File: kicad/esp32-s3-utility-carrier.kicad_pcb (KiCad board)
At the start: 2 copper layers, 130 x 85 mm, 30 parts, among them SW1 BTN1, SW2 BTN2, SW3 BTN3, U2 SN74AHCT125N

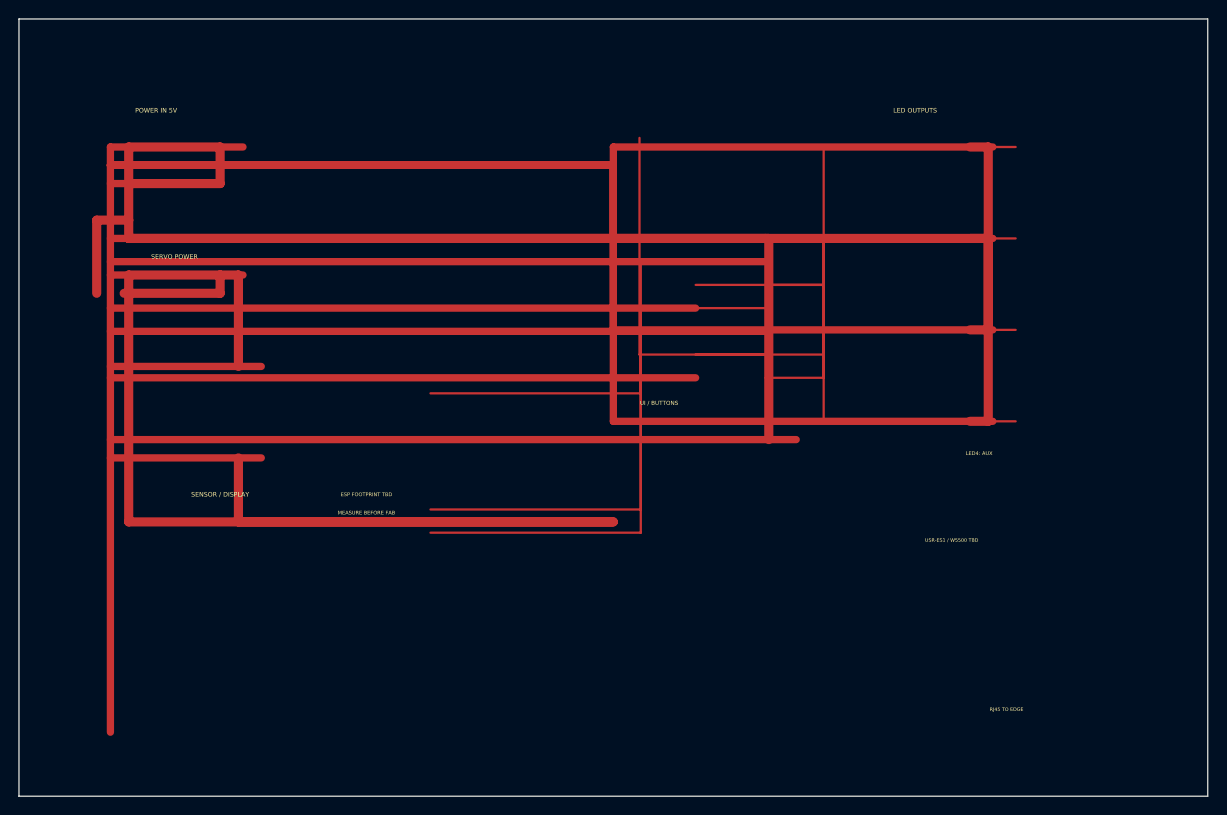
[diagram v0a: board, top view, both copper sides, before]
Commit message: fix(pcb): replace messy routing with LED data routing only
Revert v0.7 board-wide power traces; keep v0.7 placement. Route thin
LED data chain and short C_AHCT at U2 with 45° bends outside ESP keep-outs.

Co-authored-by: Cursor <cursoragent@cursor.com>
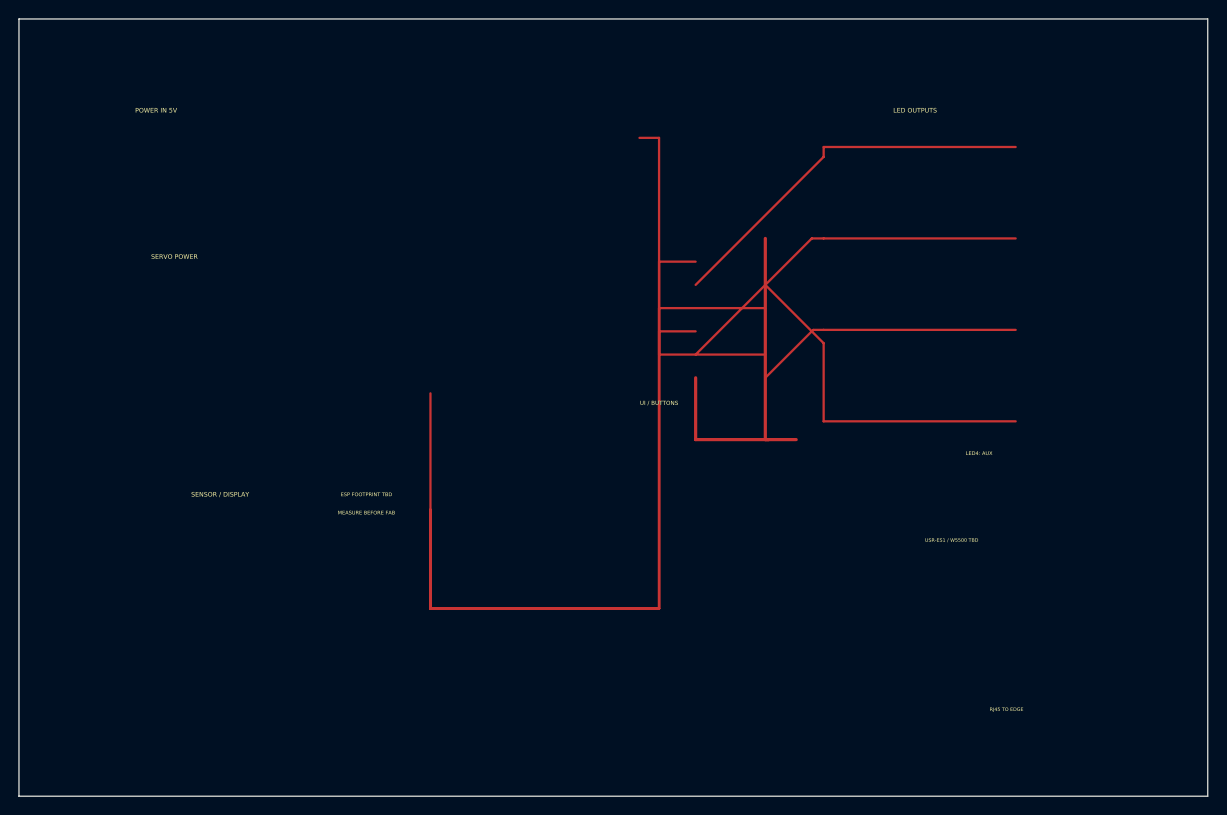
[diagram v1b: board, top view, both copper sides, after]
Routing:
- net GND: track 984.2 -> 17.8 mm
- net 5V_SERVO: track 162.5 -> 0.00 mm
- net 5V_LED: track 142.0 -> 0.00 mm
- net 5V_LOGIC: track 94.0 -> 22.4 mm
- net LED4_IN: track 45.9 -> 93.1 mm
- net 5V_MAIN: track 43.5 -> 0.00 mm
- net LED2_IN: track 48.5 -> 70.2 mm
- net LED1_IN: track 58.6 -> 75.3 mm
- net LED1_DATA: track 50.1 -> 41.9 mm
- net LED2_DATA: track 47.7 -> 40.3 mm
- net LED4_DATA: track 42.3 -> 38.6 mm
- net LED3_DATA: track 32.6 -> 29.6 mm
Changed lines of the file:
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@@
     (property "Footprint" "carrier:JST_W5500_1x08_Placeholder")
     (attr through_hole)
-  )  (segment (start 12 18) (end 12.0 18) (width 1.0) (layer "F.Cu") (net 1))
-  (segment (start 12.0 18) (end 22 18) (width 1.0) (layer "F.Cu") (net 1))
-  (segment (start 22 18) (end 22 14) (width 1.0) (layer "F.Cu") (net 1))
-  (segment (start 15.96 18) (end 10.0 18) (width 0.8) (layer "F.Cu") (net 2))
-  (segment (start 24.5 14) (end 10.0 14) (width 0.8) (layer "F.Cu") (net 2))
-  (segment (start 22 14) (end 12.0 14) (width 1.0) (layer "F.Cu") (net 1))
-  (segment (start 12.0 14) (end 12.0 22) (width 1.0) (layer "F.Cu") (net 1))
-  (segment (start 12.0 22) (end 8.5 22) (width 1.0) (layer "F.Cu") (net 1))
-  (segment (start 8.5 22) (end 8.5 30) (width 1.0) (layer "F.Cu") (net 1))
-  (segment (start 12.0 22) (end 12.0 24) (width 1.0) (layer "F.Cu") (net 3))
-  (segment (start 12.0 24) (end 81.62 24) (width 1.0) (layer "F.Cu") (net 3))
-  (segment (start 81.62 24) (end 82 24) (width 1.0) (layer "F.Cu") (net 3))
-  (segment (start 82 24) (end 82 46) (width 1.0) (layer "F.Cu") (net 3))
-  (segment (start 85.0 46) (end 10.0 46) (width 0.8) (layer "F.Cu") (net 2))
-  (segment (start 74 39.24) (end 10.0 39.24) (width 0.8) (layer "F.Cu") (net 2))
-  (segment (start 74 24) (end 10.0 24) (width 0.8) (layer "F.Cu") (net 2))
-  (segment (start 74 31.62) (end 10.0 31.62) (width 0.8) (layer "F.Cu") (net 2))
-  (segment (start 81.62 34.16) (end 10.0 34.16) (width 0.8) (layer "F.Cu") (net 2))
-  (segment (start 81.62 26.54) (end 10.0 26.54) (width 0.8) (layer "F.Cu") (net 2))
-  (segment (start 11.5 30) (end 22 30) (width 1.0) (layer "F.Cu") (net 5))
-  (segment (start 22 30) (end 22 28) (width 1.0) (layer "F.Cu") (net 5))
-  (segment (start 24.5 28) (end 10.0 28) (width 0.8) (layer "F.Cu") (net 2))
-  (segment (start 22 28) (end 24 28) (width 1.0) (layer "F.Cu") (net 5))
-  (segment (start 24 28) (end 24 38) (width 1.0) (layer "F.Cu") (net 5))
-  (segment (start 26.5 38) (end 10.0 38) (width 0.8) (layer "F.Cu") (net 2))
-  (segment (start 22 28) (end 12.0 28) (width 1.0) (layer "F.Cu") (net 5))
-  (segment (start 12.0 28) (end 12.0 55) (width 1.0) (layer "F.Cu") (net 5))
-  (segment (start 12.0 55) (end 65 55) (width 1.0) (layer "F.Cu") (net 5))
-  (segment (start 65 55) (end 24 55) (width 1.0) (layer "F.Cu") (net 5))
-  (segment (start 24 55) (end 24 48) (width 1.0) (layer "F.Cu") (net 5))
-  (segment (start 26.5 48) (end 10.0 48) (width 0.8) (layer "F.Cu") (net 2))
-  (segment (start 106.0 24) (end 106.0 14) (width 1.0) (layer "F.Cu") (net 4))
-  (segment (start 106.0 14) (end 104 14) (width 1.0) (layer "F.Cu") (net 4))
-  (segment (start 106.5 14) (end 65.0 14) (width 0.8) (layer "F.Cu") (net 2))
-  (segment (start 65.0 14) (end 65.0 16) (width 0.8) (layer "F.Cu") (net 2))
-  (segment (start 65.0 16) (end 10.0 16) (width 0.8) (layer "F.Cu") (net 2))
-  (segment (start 106.0 24) (end 106.0 24) (width 1.0) (layer "F.Cu") (net 4))
-  (segment (start 106.0 24) (end 104 24) (width 1.0) (layer "F.Cu") (net 4))
-  (segment (start 106.5 24) (end 65.0 24) (width 0.8) (layer "F.Cu") (net 2))
-  (segment (start 65.0 24) (end 65.0 16) (width 0.8) (layer "F.Cu") (net 2))
-  (segment (start 65.0 16) (end 10.0 16) (width 0.8) (layer "F.Cu") (net 2))
-  (segment (start 106.0 24) (end 106.0 34) (width 1.0) (layer "F.Cu") (net 4))
-  (segment (start 106.0 34) (end 104 34) (width 1.0) (layer "F.Cu") (net 4))
-  (segment (start 106.5 34) (end 65.0 34) (width 0.8) (layer "F.Cu") (net 2))
-  (segment (start 65.0 34) (end 65.0 16) (width 0.8) (layer "F.Cu") (net 2))
-  (segment (start 65.0 16) (end 10.0 16) (width 0.8) (layer "F.Cu") (net 2))
-  (segment (start 106.0 24) (end 106.0 44) (width 1.0) (layer "F.Cu") (net 4))
-  (segment (start 106.0 44) (end 104 44) (width 1.0) (layer "F.Cu") (net 4))
-  (segment (start 106.5 44) (end 65.0 44) (width 0.8) (layer "F.Cu") (net 2))
-  (segment (start 65.0 44) (end 65.0 16) (width 0.8) (layer "F.Cu") (net 2))
-  (segment (start 65.0 16) (end 10.0 16) (width 0.8) (layer "F.Cu") (net 2))
-  (segment (start 12.0 24) (end 106.0 24) (width 1.0) (layer "F.Cu") (net 4))
-  (segment (start 45 56.18) (end 68.0 56.18) (width 0.25) (layer "F.Cu") (net 7))
-  (segment (start 68.0 56.18) (end 68.0 26.54) (width 0.25) (layer "F.Cu") (net 7))
-  (segment (start 68.0 26.54) (end 74 26.54) (width 0.25) (layer "F.Cu") (net 7))
-  (segment (start 74 29.08) (end 88 29.08) (width 0.25) (layer "F.Cu") (net 8))
-  (segment (start 88 29.08) (end 88 14) (width 0.25) (layer "F.Cu") (net 8))
-  (segment (start 88 14) (end 100.0 14) (width 0.25) (layer "F.Cu") (net 8))
-  (segment (start 100.0 14) (end 109.0 14) (width 0.25) (layer "F.Cu") (net 8))
-  (segment (start 45 53.64) (end 68.0 53.64) (width 0.25) (layer "F.Cu") (net 9))
-  (segment (start 68.0 53.64) (end 68.0 34.16) (width 0.25) (layer "F.Cu") (net 9))
-  (segment (start 68.0 34.16) (end 74 34.16) (width 0.25) (layer "F.Cu") (net 9))
-  (segment (start 74 36.7) (end 88 36.7) (width 0.25) (layer "F.Cu") (net 10))
-  (segment (start 88 36.7) (end 88 24) (width 0.25) (layer "F.Cu") (net 10))
-  (segment (start 88 24) (end 100.0 24) (width 0.25) (layer "F.Cu") (net 10))
-  (segment (start 100.0 24) (end 109.0 24) (width 0.25) (layer "F.Cu") (net 10))
-  (segment (start 67.86 13.0) (end 67.86 36.7) (width 0.25) (layer "F.Cu") (net 11))
-  (segment (start 67.86 36.7) (end 68.0 36.7) (width 0.25) (layer "F.Cu") (net 11))
-  (segment (start 68.0 36.7) (end 81.62 36.7) (width 0.25) (layer "F.Cu") (net 11))
-  (segment (start 81.62 39.24) (end 88 39.24) (width 0.25) (layer "F.Cu") (net 12))
-  (segment (start 88 39.24) (end 88 34) (width 0.25) (layer "F.Cu") (net 12))
-  (segment (start 88 34) (end 100.0 34) (width 0.25) (layer "F.Cu") (net 12))
-  (segment (start 100.0 34) (end 109.0 34) (width 0.25) (layer "F.Cu") (net 12))
-  (segment (start 45 40.94) (end 68.0 40.94) (width 0.25) (layer "F.Cu") (net 13))
-  (segment (start 68.0 40.94) (end 68.0 31.62) (width 0.25) (layer "F.Cu") (net 13))
-  (segment (start 68.0 31.62) (end 81.62 31.62) (width 0.25) (layer "F.Cu") (net 13))
-  (segment (start 81.62 29.08) (end 88 29.08) (width 0.25) (layer "F.Cu") (net 14))
-  (segment (start 88 29.08) (end 88 44) (width 0.25) (layer "F.Cu") (net 14))
-  (segment (start 88 44) (end 100.0 44) (width 0.25) (layer "F.Cu") (net 14))
-  (segment (start 100.0 44) (end 109.0 44) (width 0.25) (layer "F.Cu") (net 14))
-  (segment (start 10.0 14) (end 10.0 78) (width 0.8) (layer "F.Cu") (net 2))
+  )  (segment (start 45 56.18) (end 45 64.5) (width 0.25) (layer "F.Cu") (net 7))
+  (segment (start 45 64.5) (end 70.0 64.5) (width 0.25) (layer "F.Cu") (net 7))
+  (segment (start 70.0 64.5) (end 70.0 26.54) (width 0.25) (layer "F.Cu") (net 7))
+  (segment (start 70.0 26.54) (end 74 26.54) (width 0.25) (layer "F.Cu") (net 7))
+  (segment (start 74 29.08) (end 88.0 15.079999999999998) (width 0.25) (layer "F.Cu") (net 8))
+  (segment (start 88.0 15.079999999999998) (end 88 14) (width 0.25) (layer "F.Cu") (net 8))
+  (segment (start 88 14) (end 109.0 14) (width 0.25) (layer "F.Cu") (net 8))
+  (segment (start 45 53.64) (end 45 64.5) (width 0.25) (layer "F.Cu") (net 9))
+  (segment (start 45 64.5) (end 70.0 64.5) (width 0.25) (layer "F.Cu") (net 9))
+  (segment (start 70.0 64.5) (end 70.0 34.16) (width 0.25) (layer "F.Cu") (net 9))
+  (segment (start 70.0 34.16) (end 74 34.16) (width 0.25) (layer "F.Cu") (net 9))
+  (segment (start 74 36.7) (end 86.7 24.0) (width 0.25) (layer "F.Cu") (net 10))
+  (segment (start 86.7 24.0) (end 88 24) (width 0.25) (layer "F.Cu") (net 10))
+  (segment (start 88 24) (end 109.0 24) (width 0.25) (layer "F.Cu") (net 10))
+  (segment (start 67.86 13.0) (end 70.0 13.0) (width 0.25) (layer "F.Cu") (net 11))
+  (segment (start 70.0 13.0) (end 70.0 36.7) (width 0.25) (layer "F.Cu") (net 11))
+  (segment (start 70.0 36.7) (end 81.62 36.7) (width 0.25) (layer "F.Cu") (net 11))
+  (segment (start 81.62 39.24) (end 86.86000000000001 34.0) (width 0.25) (layer "F.Cu") (net 12))
+  (segment (start 86.86000000000001 34.0) (end 88 34) (width 0.25) (layer "F.Cu") (net 12))
+  (segment (start 88 34) (end 109.0 34) (width 0.25) (layer "F.Cu") (net 12))
+  (segment (start 45 40.94) (end 45 64.5) (width 0.25) (layer "F.Cu") (net 13))
+  (segment (start 45 64.5) (end 70.0 64.5) (width 0.25) (layer "F.Cu") (net 13))
+  (segment (start 70.0 64.5) (end 70.0 31.62) (width 0.25) (layer "F.Cu") (net 13))
+  (segment (start 70.0 31.62) (end 81.62 31.62) (width 0.25) (layer "F.Cu") (net 13))
+  (segment (start 81.62 29.08) (end 88.0 35.459999999999994) (width 0.25) (layer "F.Cu") (net 14))
+  (segment (start 88.0 35.459999999999994) (end 88 44) (width 0.25) (layer "F.Cu") (net 14))
+  (segment (start 88 44) (end 109.0 44) (width 0.25) (layer "F.Cu") (net 14))
+  (segment (start 81.62 24) (end 81.62 46) (width 0.35) (layer "F.Cu") (net 3))
+  (segment (start 81.62 46) (end 82 46) (width 0.35) (layer "F.Cu") (net 3))
+  (segment (start 74 39.24) (end 74 46) (width 0.35) (layer "F.Cu") (net 2))
+  (segment (start 74 46) (end 85.0 46) (width 0.35) (layer "F.Cu") (net 2))
 )

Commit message: refactor(pcb): simplify carrier around external controls and 3 LED outputs
Co-authored-by: Cursor <cursoragent@cursor.com>
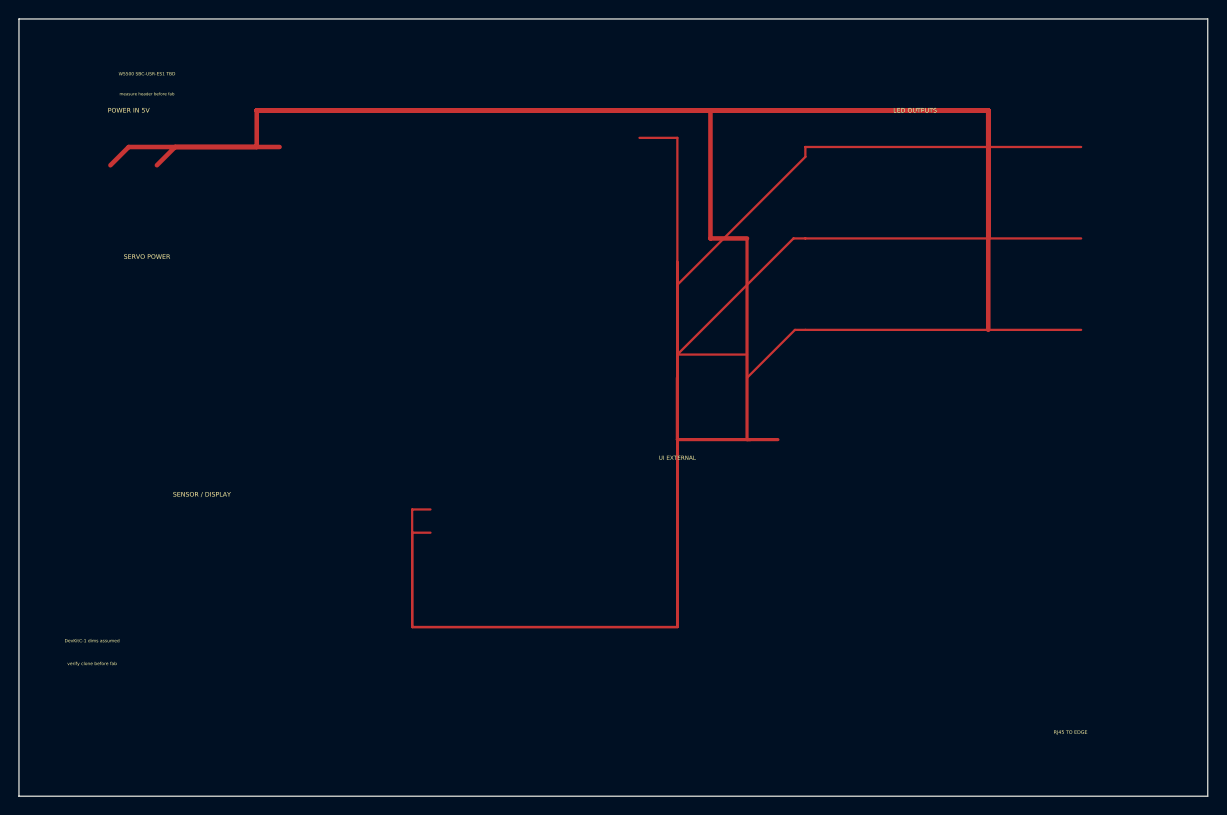
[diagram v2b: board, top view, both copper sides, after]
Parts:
- removed J_LED4: LED4_AUX, carrier:JST_XH_1x03_Placeholder
- removed the J_MAIN at (12.0, 18.0)
- removed R_LED4: 330, Resistor_THT:R_AXIAL-0.4_D5.1mm_L12.0mm_Horizontal
- removed SW1: BTN1, Button_Switch_THT:SW_PUSH_6mm
- removed SW2: BTN2, Button_Switch_THT:SW_PUSH_6mm
- removed SW3: BTN3, Button_Switch_THT:SW_PUSH_6mm
- added J_MAIN: 5V_MAIN_IN, carrier:ScrewTerm_2p_5.08_Placeholder, F.Cu at (10.0, 16.0)
- J_LED1, J_LED2, J_LED3: footprint carrier:JST_XH_1x03_Placeholder -> carrier:ScrewTerm_3p_5.08_Placeholder
- J_W5500: footprint carrier:JST_W5500_1x08_Placeholder -> carrier:W5500_SBC_USR_ES1_Placeholder
- moved J_BTN 7.00 mm to (70.0, 55.0)
- moved J_ENC 4.12 mm to (84.0, 62.0)
- moved C_MAIN 4.00 mm to (26.0, 14.0)
- moved J_W5500 3.61 mm to (100.0, 64.0)
- moved C_AHCT 2.00 mm to (80.0, 46.0)
- moved J_LED1 2.00 mm to (106.0, 14.0)
- moved J_LED2 2.00 mm to (106.0, 24.0)
- moved J_LED3 2.00 mm to (106.0, 34.0)
- moved R_LED1 2.00 mm to (86.0, 14.0)
- moved R_LED2 2.00 mm to (86.0, 24.0)
- moved R_LED3 2.00 mm to (86.0, 34.0)
- moved U2 2.00 mm to (72.0, 24.0)
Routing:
- net 5V_LED: track 0.00 -> 282.0 mm
- net LED4_IN: track 93.1 -> 0.00 mm
- net 5V_LOGIC: track 22.4 -> 94.0 mm
- net LED4_DATA: track 38.6 -> 0.00 mm
- net 5V_MAIN: track 0.00 -> 16.8 mm
- net GND: track 17.8 -> 32.0 mm
- net LED2_DATA: track 40.3 -> 49.4 mm
- net LED1_DATA: track 41.9 -> 51.0 mm
- net LED3_DATA: track 29.6 -> 38.7 mm
- net LED2_IN: track 70.2 -> 76.2 mm
- net LED1_IN: track 75.3 -> 81.3 mm
- net LED3_IN: track 37.5 -> 35.5 mm
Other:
- board text added: "DevKitC-1 dims assumed"
- board text added: "UI EXTERNAL"
- board text added: "W5500 SBC-USR-ES1 TBD"
- board text added: "measure header before fab"
- board text added: "verify clone before fab"
- board text removed: "ESP FOOTPRINT TBD"
- board text removed: "LED4: AUX"
- board text removed: "MEASURE BEFORE FAB"
- board text removed: "UI / BUTTONS"
- board text removed: "USR-ES1 / W5500 TBD"

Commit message: fix(pcb): clean visible routing after v0.9 refactor
Co-authored-by: Cursor <cursoragent@cursor.com>
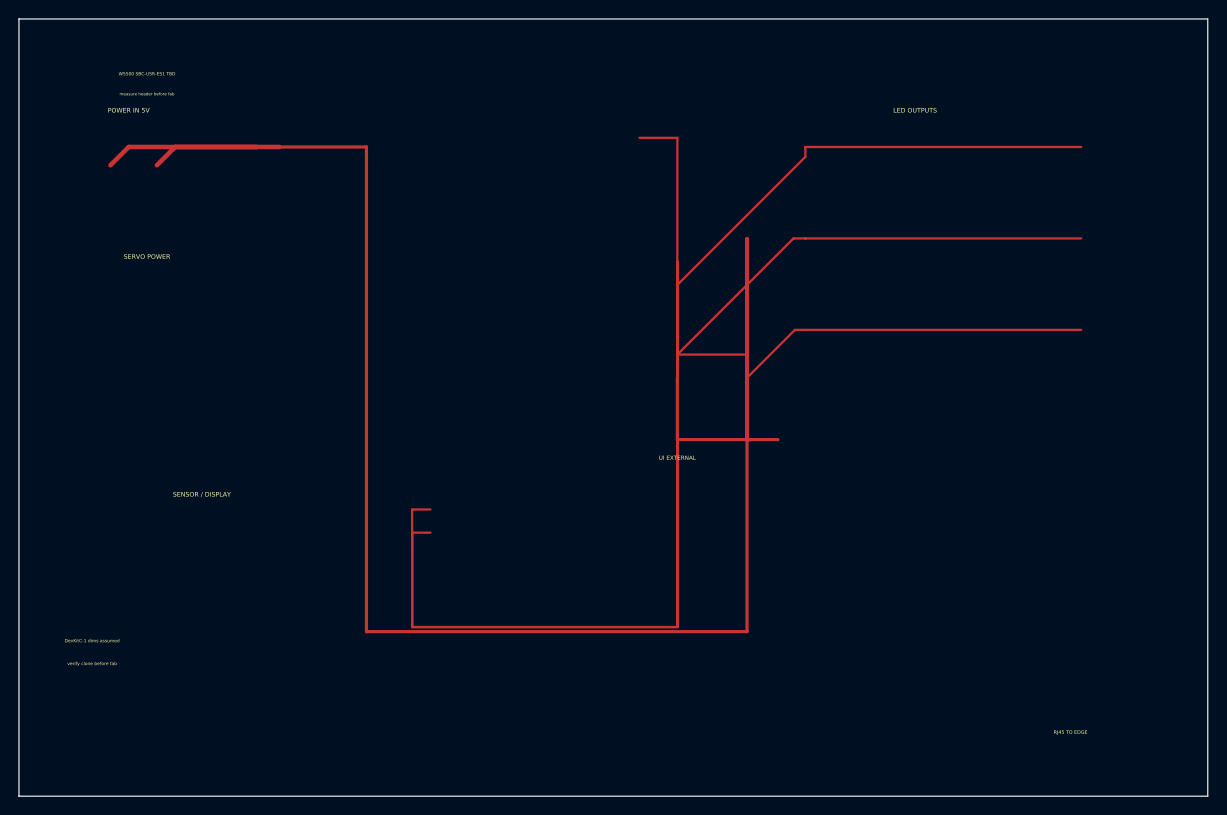
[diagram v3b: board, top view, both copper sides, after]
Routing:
- net 5V_LED: track 282.0 -> 0.00 mm
- net 5V_LOGIC: track 94.0 -> 172.0 mm
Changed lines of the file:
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@@
   (segment (start 15.08 16) (end 17.08 14.0) (width 0.5) (layer "F.Cu") (net 2))
   (segment (start 17.08 14.0) (end 28.5 14) (width 0.5) (layer "F.Cu") (net 2))
-  (segment (start 26 14) (end 26 10.0) (width 0.5) (layer "F.Cu") (net 3))
-  (segment (start 26 10.0) (end 75.62 10.0) (width 0.5) (layer "F.Cu") (net 3))
-  (segment (start 75.62 10.0) (end 75.62 24) (width 0.5) (layer "F.Cu") (net 3))
-  (segment (start 75.62 24) (end 79.62 24) (width 0.5) (layer "F.Cu") (net 3))
-  (segment (start 26 10.0) (end 106 10.0) (width 0.5) (layer "F.Cu") (net 4))
-  (segment (start 106 10.0) (end 106 14) (width 0.5) (layer "F.Cu") (net 4))
-  (segment (start 26 10.0) (end 106 10.0) (width 0.5) (layer "F.Cu") (net 4))
-  (segment (start 106 10.0) (end 106 24) (width 0.5) (layer "F.Cu") (net 4))
-  (segment (start 26 10.0) (end 106 10.0) (width 0.5) (layer "F.Cu") (net 4))
-  (segment (start 106 10.0) (end 106 34) (width 0.5) (layer "F.Cu") (net 4))
+  (segment (start 26 14) (end 38.0 14) (width 0.35) (layer "F.Cu") (net 3))
+  (segment (start 38.0 14) (end 38.0 67.0) (width 0.35) (layer "F.Cu") (net 3))
+  (segment (start 38.0 67.0) (end 79.62 67.0) (width 0.35) (layer "F.Cu") (net 3))
+  (segment (start 79.62 67.0) (end 79.62 24) (width 0.35) (layer "F.Cu") (net 3))
   (segment (start 79.62 24) (end 79.62 46) (width 0.35) (layer "F.Cu") (net 3))
   (segment (start 79.62 46) (end 80 46) (width 0.35) (layer "F.Cu") (net 3))
